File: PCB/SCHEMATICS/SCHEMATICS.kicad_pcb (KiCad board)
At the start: 2 copper layers, 69 parts, among them IC1 CP2102-GMR, Q1 PMOS, U1 C7433, U2 AMS1117-3.3, U3 LTR-303ALS-01, U4 AMS1117-3.3, U5 LTR-303ALS-01, U6 C6482, U7 C6482

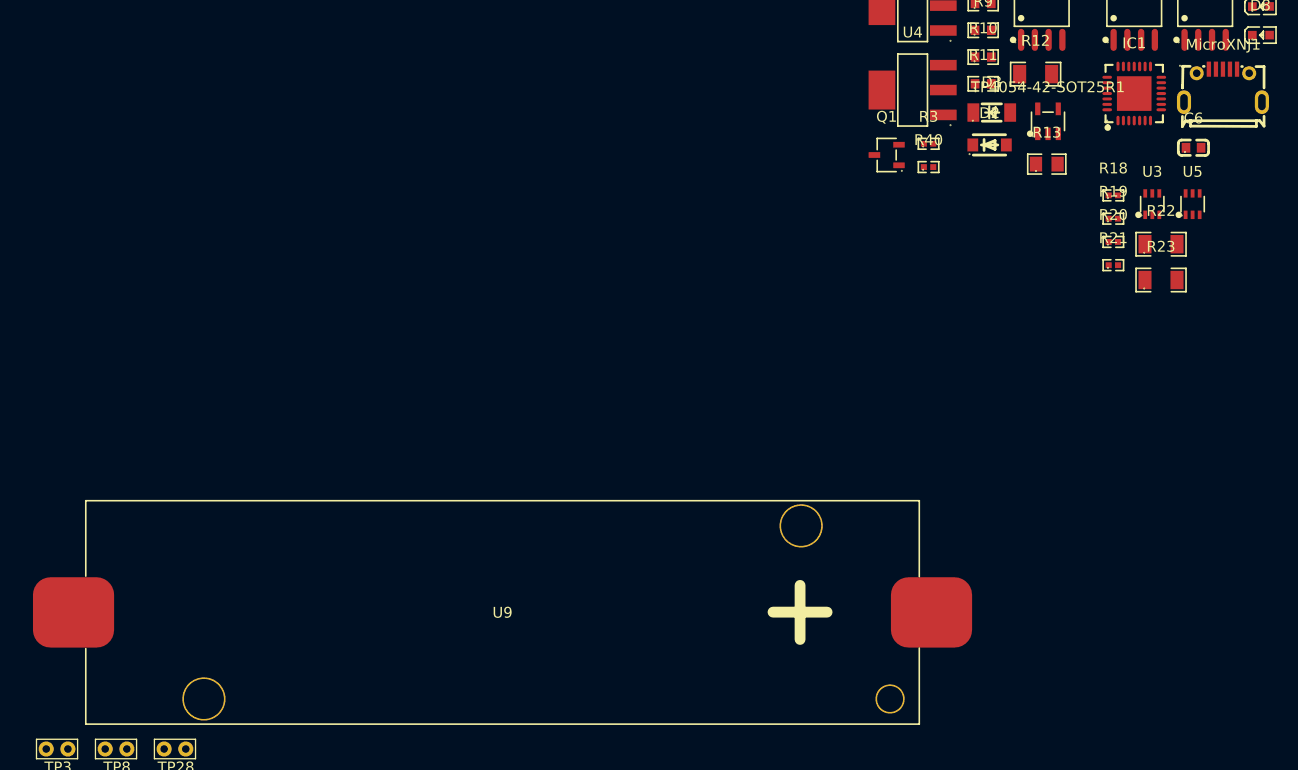
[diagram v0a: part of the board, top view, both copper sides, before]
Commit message: updated path for footprints
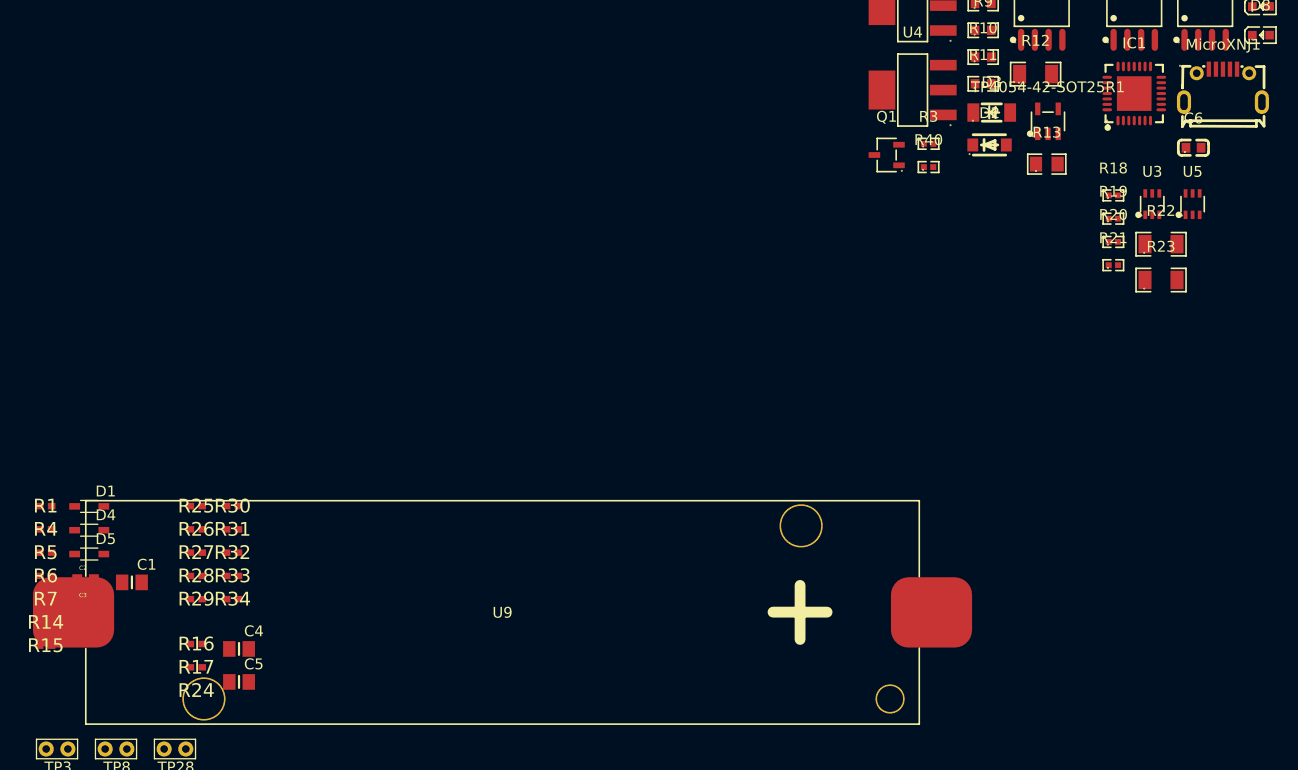
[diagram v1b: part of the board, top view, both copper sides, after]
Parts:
- added C1: 1uF, 1UF:CAPC2012X140N, F.Cu at (9.14, 7.62)
- added C2: 10uF, 10UF:CAPC1608X90N, F.Cu at (4.86, 7.36)
- added C3: 10uF, 10UF:CAPC1608X90N, F.Cu at (4.86, 9.88)
- added C4: 1uF, 1UF:CAPC2012X140N, F.Cu at (19.0, 13.8)
- added C5: 1uF, 1UF:CAPC2012X140N, F.Cu at (19.0, 16.8)
- added D1: D_Schottky, schottky:SOT323_INFINEON, F.Cu at (5.20, 0.60)
- added D4: D_Schottky, schottky:SOT323_INFINEON, F.Cu at (5.20, 2.80)
- added D5: D_Schottky, schottky:SOT323_INFINEON, F.Cu at (5.20, 5.00)
- added R1: 0, 0ohm:RESC1005X40N, F.Cu at (1.18, 0.57)
- added R14: 0, 0ohm:RESC1005X40N, F.Cu at (1.18, 11.3)
- added R15: 0, 0ohm:RESC1005X40N, F.Cu at (1.18, 13.5)
- added R16: 0, 0ohm:RESC1005X40N, F.Cu at (15.1, 13.3)
- added R17: 0, 0ohm:RESC1005X40N, F.Cu at (15.1, 15.5)
- added R24: 0, 0ohm:RESC1005X40N, F.Cu at (15.1, 17.6)
- added R25: 2.2k, 2.2k:RESC1005X40N, F.Cu at (15.1, 0.57)
- added R26: 0, 0ohm:RESC1005X40N, F.Cu at (15.1, 2.73)
- added R27: 2.2k, 2.2k:RESC1005X40N, F.Cu at (15.1, 4.88)
- added R28: 0, 0ohm:RESC1005X40N, F.Cu at (15.1, 7.03)
- added R29: 0, 0ohm:RESC1005X40N, F.Cu at (15.1, 9.18)
- added R30: 0, 0ohm:RESC1005X40N, F.Cu at (18.4, 0.57)
- added R31: 0, 0ohm:RESC1005X40N, F.Cu at (18.4, 2.73)
- added R32: 0, 0ohm:RESC1005X40N, F.Cu at (18.4, 4.88)
- added R33: 0, 0ohm:RESC1005X40N, F.Cu at (18.4, 7.03)
- added R34: 0, 0ohm:RESC1005X40N, F.Cu at (18.4, 9.18)
- added R4: 0, 0ohm:RESC1005X40N, F.Cu at (1.18, 2.73)
- added R5: 0, 0ohm:RESC1005X40N, F.Cu at (1.18, 4.88)
- added R6: 2.2k, 2.2k:RESC1005X40N, F.Cu at (1.18, 7.03)
- added R7: 0, 0ohm:RESC1005X40N, F.Cu at (1.18, 9.18)

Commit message: Fixed warning in PCB editor
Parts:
- C1, C4, C5: footprint 1UF:CAPC2012X140N -> footprint:CAPC2012X140N
- C2, C3: footprint 10UF:CAPC1608X90N -> footprint:CAPC1608X90N
- D1, D4, D5: footprint schottky:SOT323_INFINEON -> footprint:SOT323_INFINEON
- R1, R14, R15, R16, R17, R24, R26, R28, R29, R30, R31, R32, R33, R34, R4, R5, R7: footprint 0ohm:RESC1005X40N -> footprint:RESC1005X40N
- R25, R27, R6: footprint 2.2k:RESC1005X40N -> footprint:RESC1005X40N
- R40: value Value: Value: Value: Value: Value: Value: 510k -> Value: Value: 510k
- TP1, TP10, TP11, TP12, TP13, TP14, TP15, TP16, TP17, TP18, TP19, TP2, TP20, TP21, TP22, TP23, TP24, TP25, TP26, TP27, TP28, TP29, TP3, TP30, TP31, TP32, TP33, TP34, TP35, TP4, TP5, TP6, TP7, TP8, TP9: footprint TestPoint:TestPoint_Bridge_Pitch2.0mm_Drill0.7mm -> TestPoint:TestPoint_Pad_D2.0mm
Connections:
- D1 pad A: (no net) -> Net-(D1-PadA)
- D1 pad C: (no net) -> Net-(D1-K)
- D4 pad A: (no net) -> Net-(D4-PadA)
- D4 pad C: (no net) -> Net-(D2-K)
- D5 pad A: (no net) -> Net-(D5-PadA)
- D5 pad C: (no net) -> Net-(D5-K)
- R1 pad 2: Net-(D1-A) -> Net-(D1-PadA)
- R15 pad 2: Net-(D5-A) -> Net-(D5-PadA)
- R5 pad 2: Net-(D4-A) -> Net-(D4-PadA)
- TP5 pad 1: Net-(D4-A) -> Net-(D4-PadA)
- TP9 pad 1: Net-(D1-A) -> Net-(D1-PadA)
- U9 pad 1: (no net) -> /POWER MODULE/Battery
- U9 pad 2: (no net) -> GND

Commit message: Creating ratsnest
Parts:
- R40: value Value: Value: 510k -> Value: Value: Value: 510k
- moved C4 282.2 mm to (270.2, 142.4)
- moved C5 275.5 mm to (273.7, 122.1)
- moved R16 272.5 mm to (253.4, 145.3)
- moved R17 269.0 mm to (253.4, 140.3)
- moved R18 248.6 mm to (275.8, 147.5)
- moved R7 246.4 mm to (246.4, 33.0)
- moved R19 243.5 mm to (270.7, 147.5)
- moved TP6 242.8 mm to (243.8, 22.9)
- moved U3 236.4 mm to (264.2, 146.0)
- moved C3 235.5 mm to (238.0, 43.2)
- moved TP29 234.8 mm to (246.4, 43.2)
- moved TP11 227.5 mm to (231.4, 68.3)
- moved D6 226.2 mm to (99.9, 177.6)
- moved D8 226.2 mm to (99.9, 182.9)
- moved D7 226.2 mm to (99.9, 180.2)
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
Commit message: RATS NEST START
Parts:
- R40: value Value: Value: Value: 510k -> 510k
- moved U8 122.1 mm to (143.9, 101.1)
- moved D8 110.4 mm to (193.8, 124.8), turned to 90 degrees
- moved R31 107.0 mm to (194.0, 118.5), turned to 90 degrees
- moved D7 106.7 mm to (191.1, 124.8), turned to 90 degrees
- moved R29 104.9 mm to (190.0, 118.5), turned to 90 degrees
- moved R30 104.2 mm to (192.0, 118.5), turned to 90 degrees
- moved D6 103.1 mm to (188.5, 124.8), turned to 90 degrees
- moved C4 96.7 mm to (211.0, 66.0), turned to -90 degrees
- moved R18 96.6 mm to (212.0, 75.0), turned to 180 degrees
- moved TP13 94.3 mm to (199.0, 84.0)
- moved TP15 94.2 mm to (199.0, 74.0)
- moved R16 94.1 mm to (199.0, 68.5), turned to 90 degrees
- moved R17 93.3 mm to (199.0, 64.5), turned to 90 degrees
- moved U3 92.7 mm to (211.0, 70.0), turned to 90 degrees
- moved R19 88.9 mm to (208.4, 84.0), turned to 180 degrees
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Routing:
- net GND: track 0.00 -> 6.20 mm
- net Net-(D6-A): track 0.00 -> 5.66 mm
- net Net-(D7-A): track 0.00 -> 5.39 mm
- net Net-(D8-A): track 0.00 -> 5.26 mm

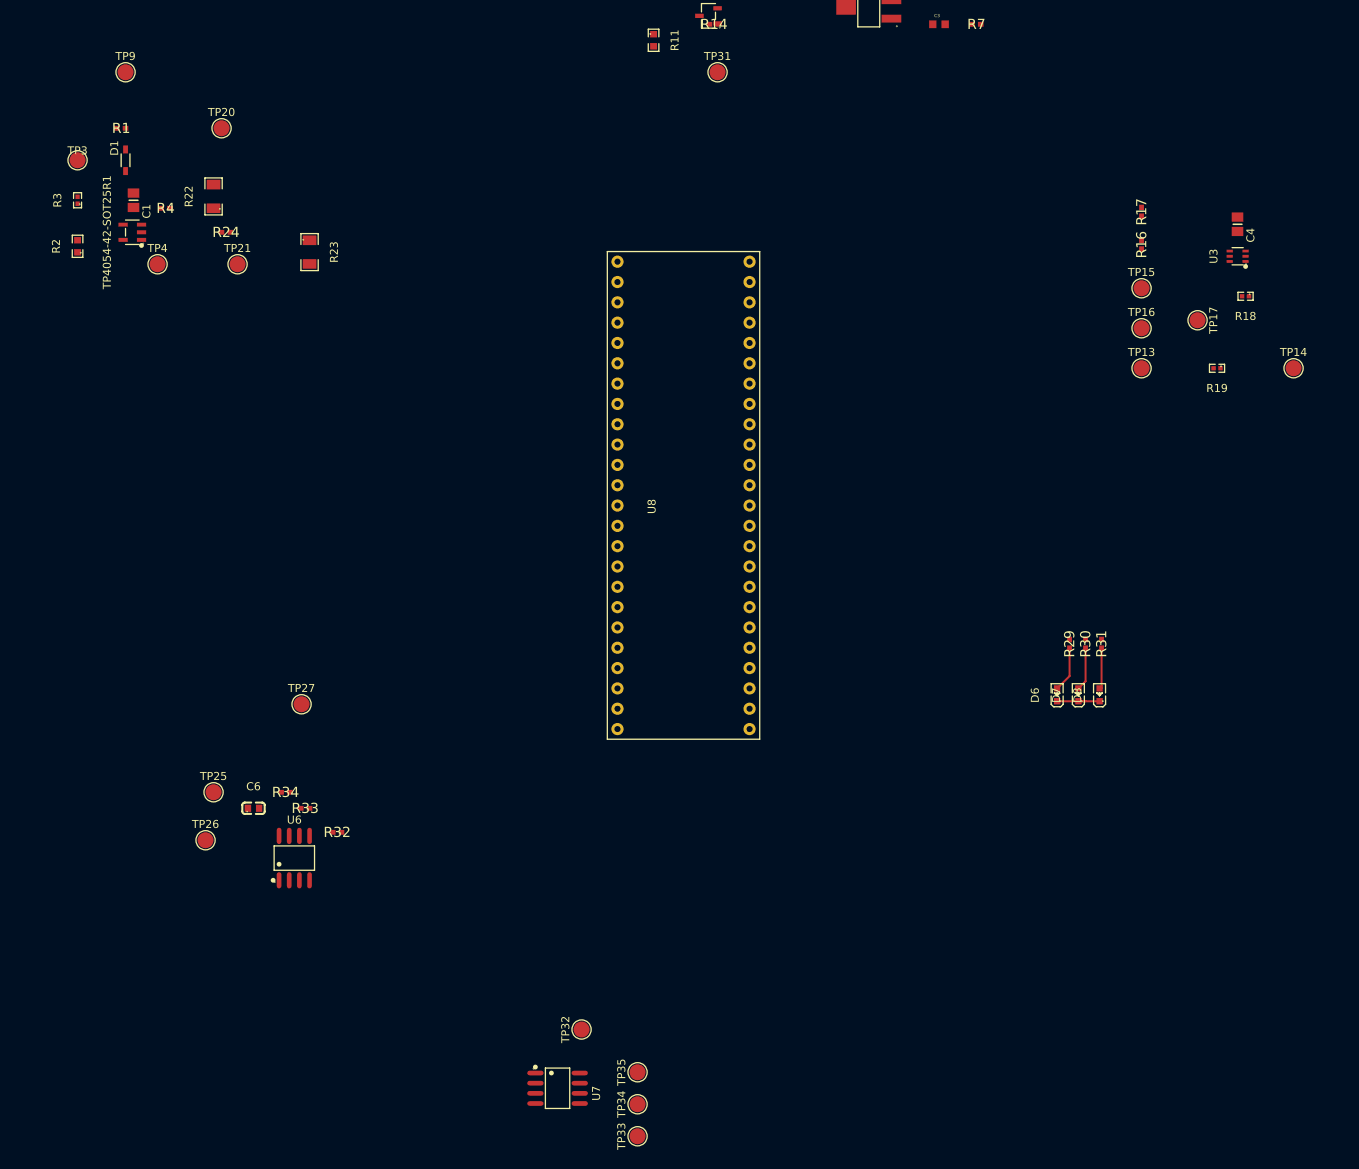
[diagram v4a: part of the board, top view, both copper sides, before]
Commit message: Added traces
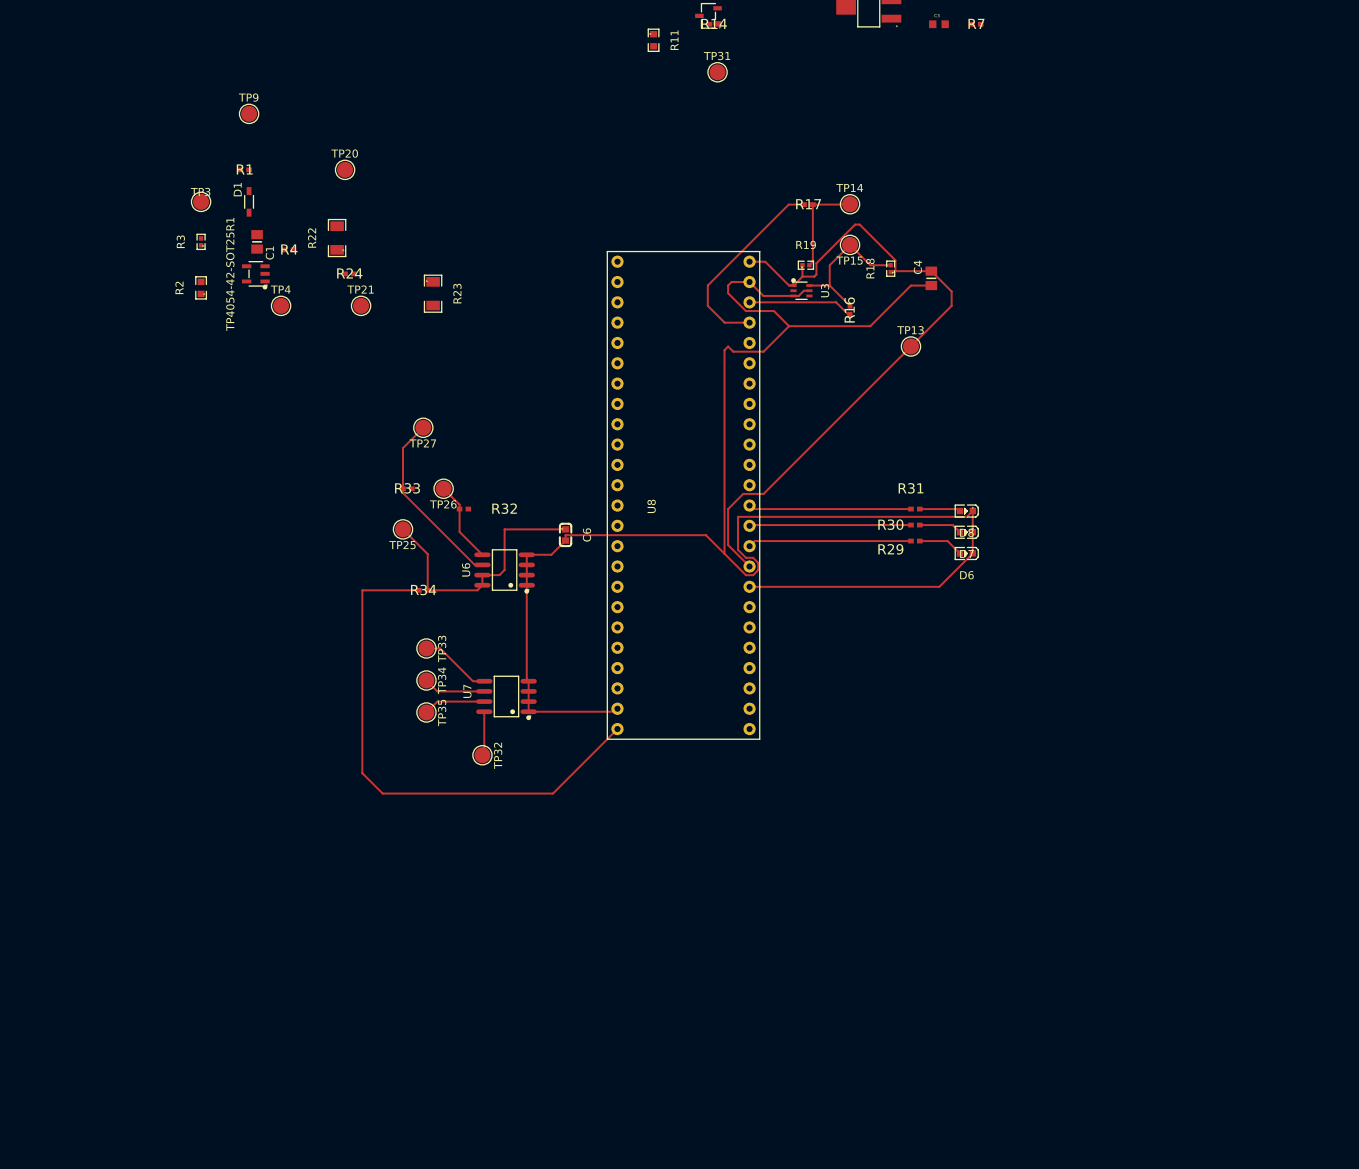
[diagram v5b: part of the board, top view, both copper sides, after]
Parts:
- removed TP16, TP17: TestPoint, TestPoint:TestPoint_Pad_D2.0mm
- R40: value 510k -> Value: Value: Value: 510k
- moved TP33 66.4 mm to (109.6, 119.0), turned to -90 degrees
- moved TP34 59.2 mm to (109.6, 123.0), turned to -90 degrees
- moved TP14 59.1 mm to (162.6, 63.5)
- moved U3 54.7 mm to (156.5, 74.3), turned to -90 degrees
- moved TP26 53.1 mm to (111.8, 99.1), turned to 180 degrees
- moved R19 53.0 mm to (157.0, 71.1), turned to 0 degrees
- moved TP35 52.1 mm to (109.6, 127.0), turned to -90 degrees
- moved C6 51.8 mm to (127.0, 104.8), turned to -90 degrees
- moved U7 49.4 mm to (119.6, 125.0), turned to 90 degrees
- moved U6 44.6 mm to (119.4, 109.2), turned to 90 degrees
- moved R18 44.5 mm to (167.6, 71.6), turned to 90 degrees
- moved R32 43.4 mm to (114.3, 101.6), turned to 0 degrees
- moved R33 41.9 mm to (107.2, 99.1)
- moved R17 41.6 mm to (157.4, 63.5), turned to 0 degrees
- moved TP25 40.5 mm to (106.7, 104.1), turned to 180 degrees
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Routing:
- net GND: track 6.20 -> 214.2 mm
- net /MICROCONTROLLER/VSS: track 0.00 -> 152.2 mm
- net Net-(U6-VCC): track 0.00 -> 33.0 mm
- net /MICROCONTROLLER/PB10: track 0.00 -> 24.9 mm
- net Net-(U6-SCL): track 0.00 -> 22.9 mm
- net /MICROCONTROLLER/PA0: track 0.00 -> 20.4 mm
- net /MICROCONTROLLER/PA2: track 0.00 -> 20.4 mm
- net /MICROCONTROLLER/PA1: track 0.00 -> 20.2 mm
- net Net-(U3-SDA): track 0.00 -> 18.4 mm
- net /MICROCONTROLLER/PB11: track 0.00 -> 13.2 mm
- net Net-(U3-SCL): track 0.00 -> 12.4 mm
- net Net-(U6-SDA): track 0.00 -> 10.3 mm
- net Net-(U7-SDA): track 0.00 -> 8.92 mm
- net Net-(U7-SCL): track 0.00 -> 7.79 mm
- net Net-(U7-WP): track 0.00 -> 7.79 mm
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
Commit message: Updating PCB
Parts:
- R40: value Value: Value: Value: 510k -> 510k
- moved TP18 67.7 mm to (201.7, 36.6)
- moved C5 56.7 mm to (211.7, 36.6), turned to 180 degrees
- moved U5 48.4 mm to (211.8, 42.2), turned to -90 degrees
- moved R21 44.5 mm to (217.9, 45.7), turned to 180 degrees
- moved R20 43.6 mm to (217.9, 41.1)
- moved TP9 42.8 mm to (53.8, 78.7)
- moved TP1 42.4 mm to (217.4, 34.5)
- moved R23 41.4 mm to (69.6, 81.3)
- moved R1 38.4 mm to (49.8, 69.1)
- moved TP2 36.6 mm to (212.9, 50.8)
- moved TP19 36.6 mm to (224.5, 41.1)
- moved R24 32.9 mm to (70.1, 85.9)
- moved D1 32.3 mm to (55.7, 69.1), turned to 180 degrees
- moved TP20 29.2 mm to (82.3, 82.8)
- moved IC1 28.4 mm to (42.7, 63.5), turned to -90 degrees
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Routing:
- net /POWER MODULE/Battery: track 0.00 -> 278.4 mm
- net GND: track 214.2 -> 464.4 mm
- net /MICROCONTROLLER/VSS: track 152.2 -> 329.9 mm
- net /MICROCONTROLLER/PA11: track 0.00 -> 106.8 mm
- net /MICROCONTROLLER/PA12: track 0.00 -> 104.3 mm
- net Net-(#FLG06-pwr): track 0.00 -> 59.1 mm
- net Net-(#FLG05-pwr): track 0.00 -> 32.8 mm
- net Net-(TP4054-42-SOT25R1-BAT): track 0.00 -> 23.1 mm
- net /MICROCONTROLLER/5V: track 0.00 -> 18.9 mm
- net Net-(R22-Pad1): track 0.00 -> 16.9 mm
- net Net-(D3-K): track 0.00 -> 16.9 mm
- net Net-(MicroXNJ1-D+): track 0.00 -> 15.3 mm
- net Net-(D1-K): track 0.00 -> 15.2 mm
- net Net-(MicroXNJ1-D-): track 0.00 -> 14.4 mm
- net Net-(U5-VDD): track 0.00 -> 14.1 mm
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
